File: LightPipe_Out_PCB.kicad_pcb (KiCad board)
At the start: 4 copper layers, 38.1 x 38.1 mm, 11 parts, among them J1 Conn_01x03, J2 Conn_01x02, J3 Conn_01x04, J4 Conn_01x04, J5 Conn_01x04, J6 Conn_01x01, J7 Conn_01x01, J8 Conn_01x02, J9 Conn_01x03, M1 MountingHole_3.2mm_M3, M2 MountingHole_3.2mm_M3

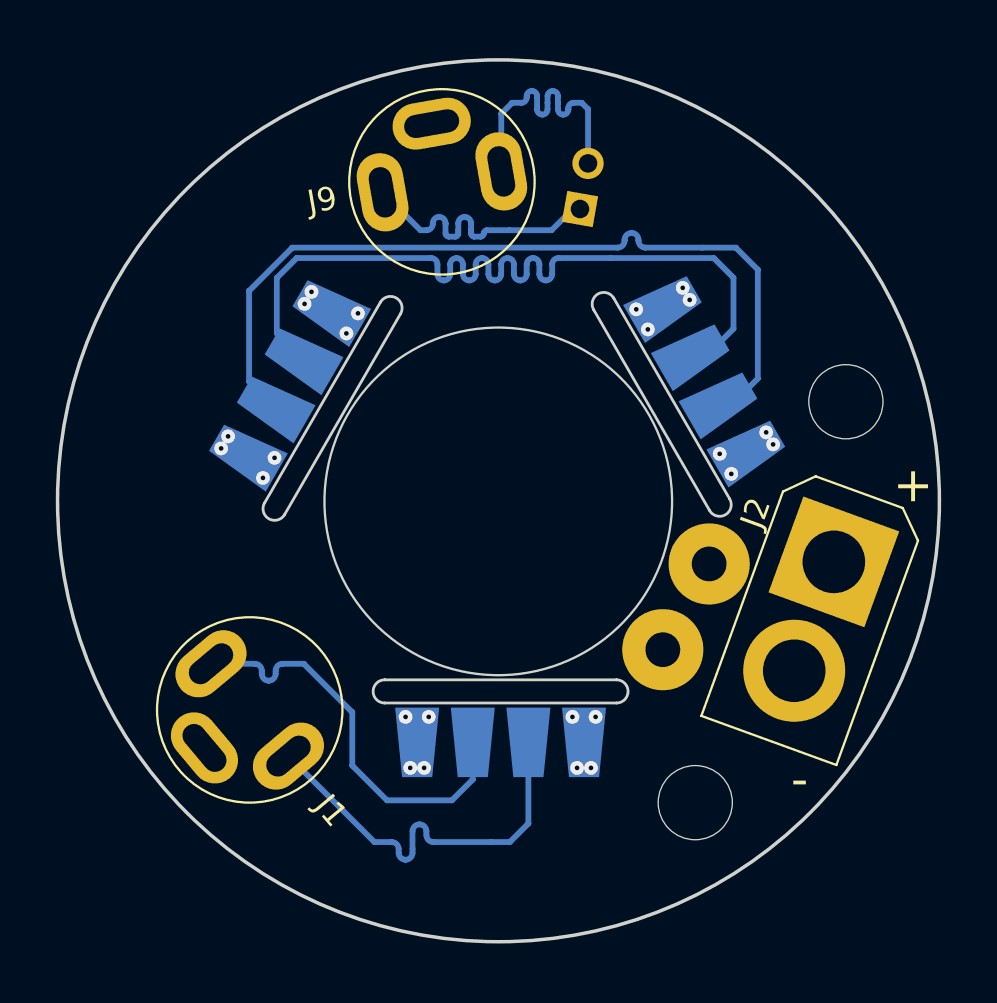
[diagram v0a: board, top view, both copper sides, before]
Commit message: [PCB] New Design features to use the PCB as In- and Out-PCB
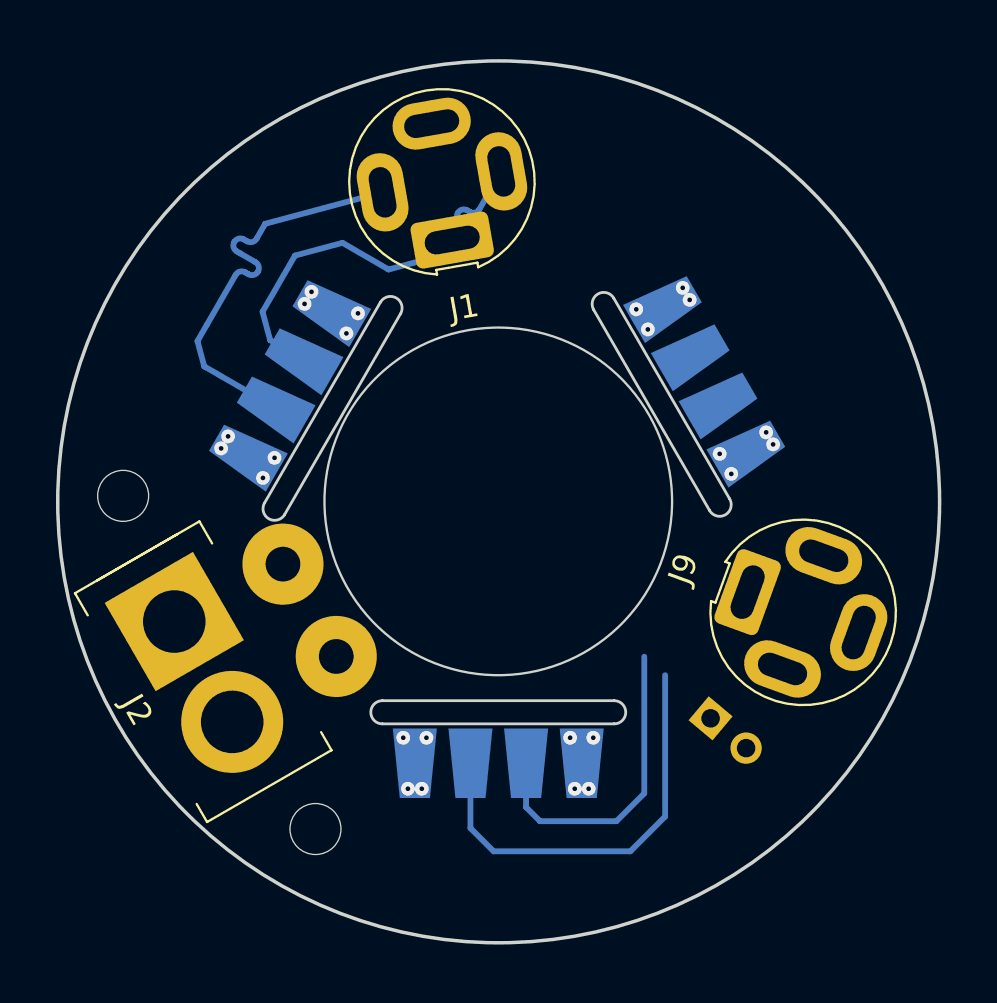
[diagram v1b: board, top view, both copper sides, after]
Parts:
- removed M2: MountingHole_3.2mm_M3, MountingHole:MountingHole_3.2mm_M3
- added REF**: MountingHole_2.2mm_M2, MountingHole:MountingHole_2.2mm_M2, F.Cu at (-16.2, -0.24)
- J1, J9: value Conn_01x03 -> Conn_01x04; footprint h8-Connectors:Lumberg-KLB-4-Klinkensteckverbinder-3_5 -> h8-Connectors:Lumberg-KLB-4-Klinkensteckverbinder-3_5-180deg-turnable
- M1: value MountingHole_3.2mm_M3 -> MountingHole_2.2mm_M2; footprint MountingHole:MountingHole_3.2mm_M3 -> MountingHole:MountingHole_2.2mm_M2
- moved M1 29.4 mm to (-7.89, 14.1), turned to -60 degrees
- moved J2 26.5 mm to (-12.7, 7.35), turned to -60 degrees
- moved J9 24.2 mm to (13.2, 4.79), turned to -110 degrees
- moved J1 24.2 mm to (-2.43, -13.8), turned to 10 degrees
- moved J8 22.7 mm to (9.16, 9.36), turned to -130 degrees
- moved J6 18.4 mm to (-9.29, 2.71), turned to -60 degrees
- moved J4 16.3 mm to (0.00, 9.80), turned to -90 degrees
- moved J3 15.4 mm to (7.66, -4.54), turned to 30 degrees
- moved J5 15.4 mm to (-7.76, -4.36), turned to 150 degrees
- moved J7 14.1 mm to (-6.99, 6.69), turned to -60 degrees
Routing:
- net /d1: track 38.0 -> 13.6 mm
- net /clk1: track 37.0 -> 18.3 mm
- net /clk3: track 12.0 -> 0.00 mm
- net /d3: track 11.9 -> 0.00 mm
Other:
- outline, holes or cut-outs redrawn
- board text removed: "+"
- board text removed: "-"

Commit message: Changed designators from J? to X? and LD? | Improved Footprints
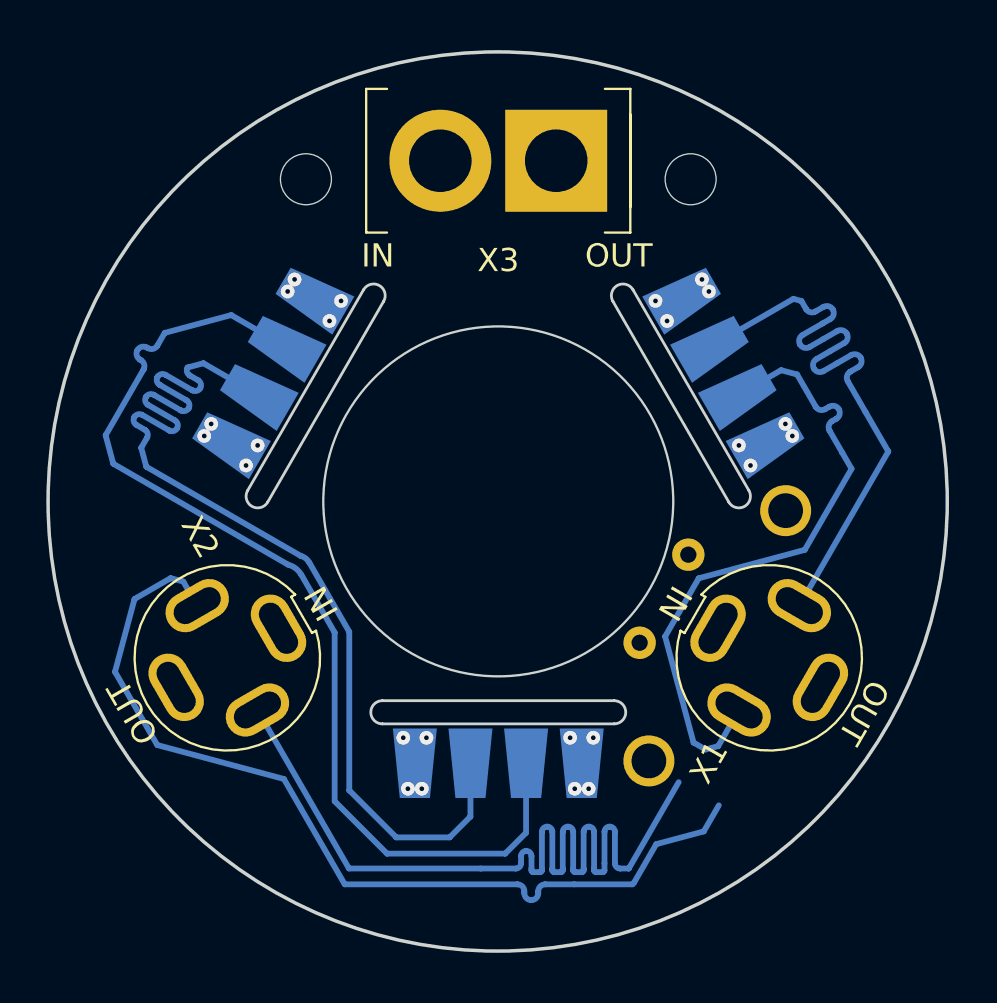
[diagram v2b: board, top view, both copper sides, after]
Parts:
- removed J8: Conn_01x02, Connector_PinHeader_2.00mm:PinHeader_1x02_P2.00mm_Vertical
- added X4.1: Conn_01x01, Connector_Wire:SolderWire-0.15sqmm_1x01_D0.5mm_OD1.5mm, B.Cu at (6.10, 6.10)
- added X4.2: Conn_01x01, Connector_Wire:SolderWire-0.15sqmm_1x01_D0.5mm_OD1.5mm, B.Cu at (8.20, 2.30)
- moved M1 28.0 mm to (-8.30, -13.9), turned to 180 degrees
- moved REF** 28.0 mm to (8.30, -13.9), turned to 180 degrees
- moved X3 25.5 mm to (0.00, -14.7), turned to 180 degrees
- moved X2 24.9 mm to (-11.7, 6.75), turned to 120 degrees
- moved X1 24.9 mm to (11.7, 6.75), turned to -120 degrees
- moved X5.1 20.4 mm to (12.4, 0.40), turned to 60 degrees
- moved X5.2 17.9 mm to (6.50, 11.2), turned to 60 degrees
- moved LD2 17.0 mm to (-8.49, -4.90), turned to 150 degrees
- moved LD3 16.3 mm to (0.00, 9.80), turned to -90 degrees
- moved LD1 16.3 mm to (8.49, -4.90), turned to 30 degrees
- renumbered J5 to LD1, J4 to LD2, J3 to LD3, J1 to X1, J9 to X2, J2 to X3, J7 to X5.1, J6 to X5.2
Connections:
- X3 pad 1: GND -> +5V
- X3 pad 2: +5V -> GND
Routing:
- net /d3: track 0.00 -> 40.0 mm
- net /clk3: track 0.00 -> 39.9 mm
- net /d1: track 13.6 -> 44.9 mm
- net /clk1: track 18.3 -> 44.9 mm
- net /d2: track 18.0 -> 28.0 mm
- net /clk2: track 17.9 -> 27.9 mm
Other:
- board size 38.1 x 38.1 mm -> 38.8 x 38.8 mm
- board text added: "IN"
- board text added: "OUT"

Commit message: [PCB] Improved footprints | optimized footprint locations | optimized wires
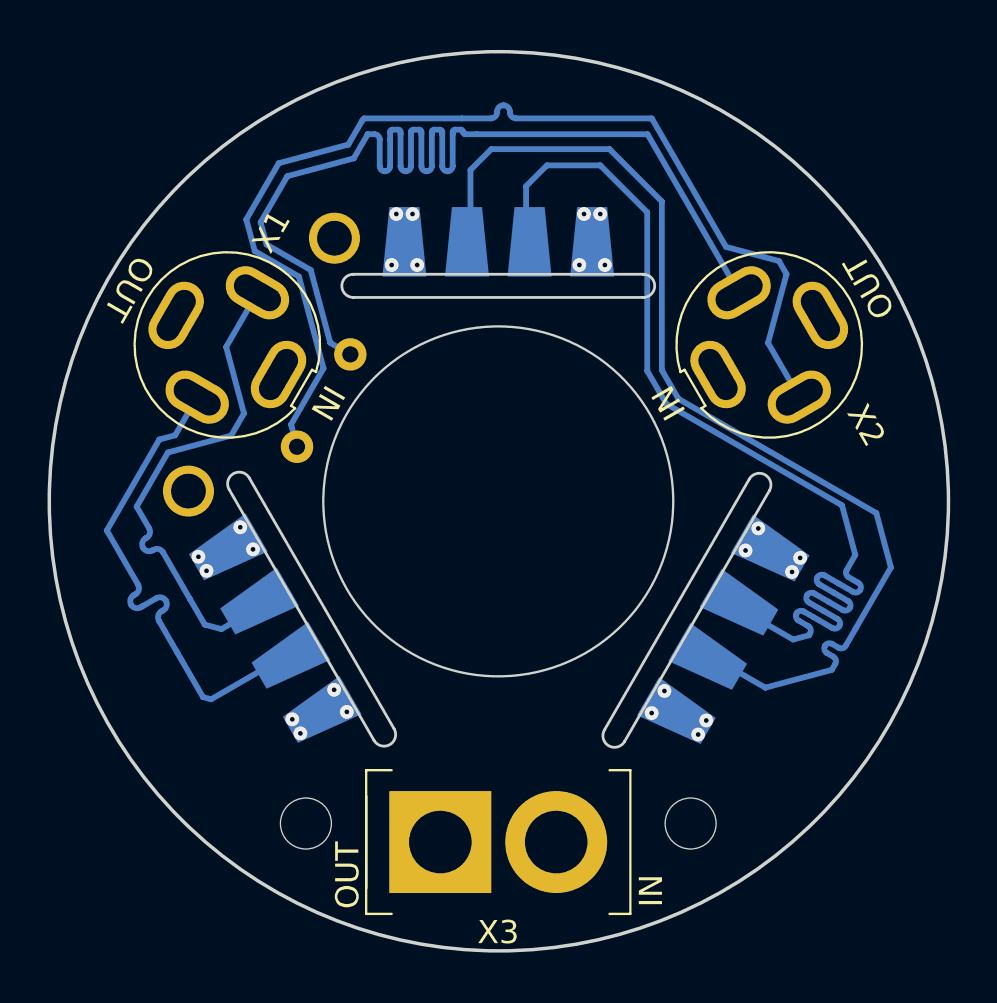
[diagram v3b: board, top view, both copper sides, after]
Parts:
- X4.1, X4.2: footprint Connector_Wire:SolderWire-0.15sqmm_1x01_D0.5mm_OD1.5mm -> h8-Connectors:Solder-Pad-THT-0.7mm
- X5.1, X5.2: footprint Connector_Wire:SolderWire-0.15sqmm_1x01_D0.5mm_OD1.5mm -> h8-Connectors:Solder-Pad-THT-1.5mm
- moved M1 32.4 mm to (8.30, 13.9), turned to 0 degrees
- moved REF** 32.4 mm to (-8.30, 13.9), turned to 0 degrees
- moved X3 29.4 mm to (0.00, 14.7), turned to 0 degrees
- moved X1 27.0 mm to (-11.7, -6.75), turned to 60 degrees
- moved X2 27.0 mm to (11.7, -6.75), turned to -60 degrees
- moved X5.2 26.3 mm to (-7.07, -11.4), turned to -120 degrees
- moved X5.1 25.8 mm to (-13.4, -0.44), turned to -120 degrees
- moved LD1 19.6 mm to (-8.49, 4.90), turned to -150 degrees
- moved LD2 19.6 mm to (8.49, 4.90), turned to -30 degrees
- moved LD3 19.6 mm to (0.00, -9.80), turned to 90 degrees
- moved X4.1 17.6 mm to (-6.38, -6.34), turned to -120 degrees
- moved X4.2 17.5 mm to (-8.68, -2.36), turned to -120 degrees
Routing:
- net /clk3: track 39.9 -> 46.9 mm
- net /d3: track 40.0 -> 47.0 mm
- net /d2: track 28.0 -> 21.5 mm
- net /clk2: track 27.9 -> 21.4 mm
- net /d1: track 44.9 -> 45.4 mm
- net /clk1: track 44.9 -> 45.5 mm
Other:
- outline, holes or cut-outs redrawn

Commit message: [doc] Create KiBot export and a basic documentation in README.md
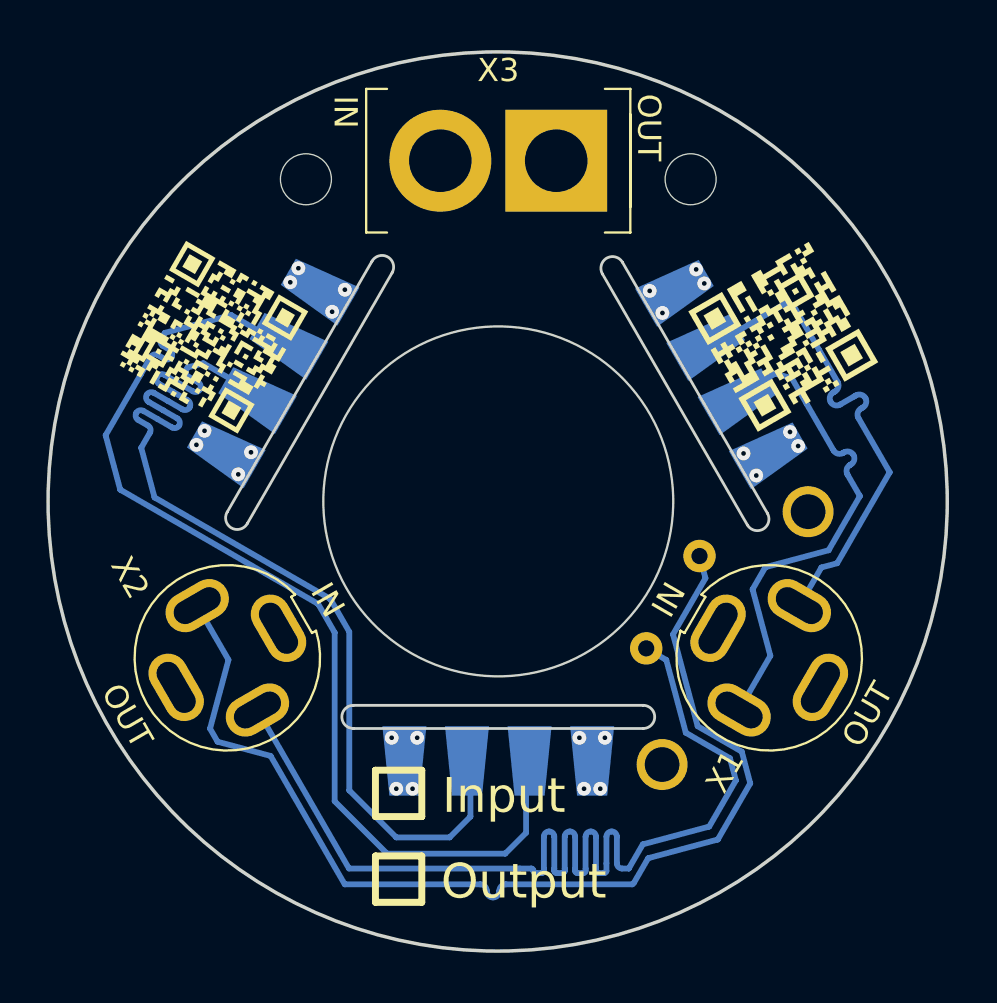
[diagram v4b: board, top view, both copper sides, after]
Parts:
- added QR***: QR_ProjecData, QR_Lib:QR_ProjecData, F.Cu at (12.3, -7.10)
- added QR***: QR_WebUrl, QR_Lib:QR_WebUrl, F.Cu at (-12.3, -7.10)
- moved M1 32.4 mm to (-8.30, -13.9), turned to 180 degrees
- moved REF** 32.4 mm to (8.30, -13.9), turned to 180 degrees
- moved X3 29.4 mm to (0.00, -14.7), turned to 180 degrees
- moved X1 27.0 mm to (11.7, 6.75), turned to -120 degrees
- moved X2 27.0 mm to (-11.7, 6.75), turned to 120 degrees
- moved X5.1 26.8 mm to (13.4, 0.44), turned to 60 degrees
- moved X5.2 26.8 mm to (7.07, 11.4), turned to 60 degrees
- moved LD1 19.6 mm to (8.49, -4.90), turned to 30 degrees
- moved LD2 19.6 mm to (-8.49, -4.90), turned to 150 degrees
- moved LD3 19.6 mm to (0.00, 9.80), turned to -90 degrees
- moved X4.2 18.0 mm to (8.68, 2.36), turned to 60 degrees
- moved X4.1 18.0 mm to (6.38, 6.34), turned to 60 degrees
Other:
- outline, holes or cut-outs redrawn
- board text added: "Input"
- board text added: "Output"

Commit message: [QR] Added QR-Code to schematic | defined QR-Code on Board to be not on schematic
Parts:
- renumbered QR*** to QR1, QR*** to QR2
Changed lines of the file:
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@@
   (footprint "QR_Lib:QR_ProjecData" (layer "F.Cu")
     (at 12.297561 -7.1 120)
-    (attr exclude_from_pos_files exclude_from_bom)
-    (fp_text reference "QR***" (at 0 4.25 120) (layer "F.SilkS") hide
+    (attr board_only exclude_from_pos_files exclude_from_bom)
+    (fp_text reference "QR1" (at 0 4.25 120) (layer "F.SilkS") hide
       (effects (font (size 1 1) (thickness 0.15)))
     )
@@
   (footprint "QR_Lib:QR_WebUrl" (layer "F.Cu")
     (at -12.297561 -7.1 -120)
-    (attr exclude_from_pos_files exclude_from_bom)
-    (fp_text reference "QR***" (at 0 4.25 60) (layer "F.SilkS") hide
+    (attr board_only exclude_from_pos_files exclude_from_bom)
+    (fp_text reference "QR2" (at 0 4.25 60) (layer "F.SilkS") hide
       (effects (font (size 1 1) (thickness 0.15)))
     )

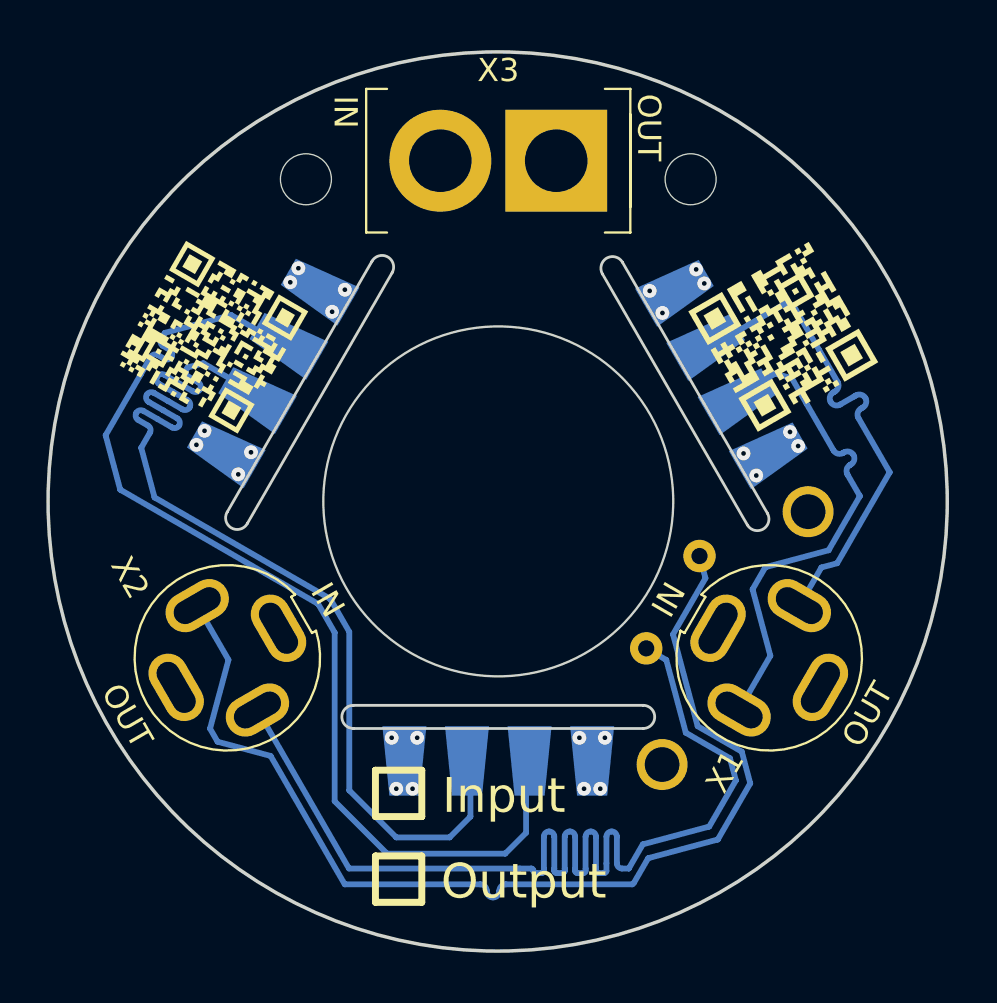
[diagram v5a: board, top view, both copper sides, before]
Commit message: [pcb] Optimized X1 and X2 positon
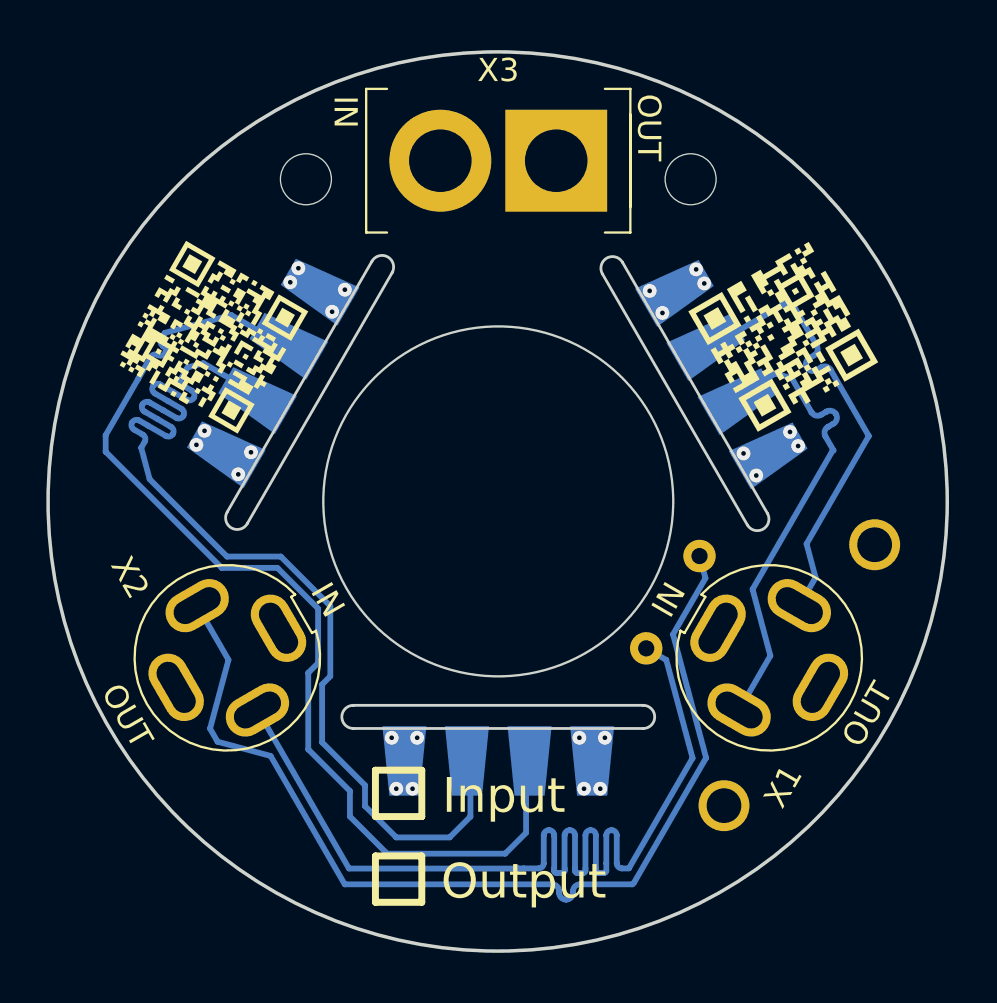
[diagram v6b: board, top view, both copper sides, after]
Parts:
- LD1, LD2, LD3: value Conn_01x04 -> APA102
- M1: renamed from REF**; value MountingHole_2.2mm_M2 -> 2.2mm_M2
- M2: renamed from M1; value MountingHole_2.2mm_M2 -> 2.2mm_M2
- X1, X2: value Conn_01x04 -> KLB-4
- X3: value Conn_01x02 -> XT30
- X4.1, X4.2: value Conn_01x01 -> Cable-0.7mm
- X5.1, X5.2: value Conn_01x01 -> Cable-1.5mm
- moved X5.1 3.21 mm to (16.2, 1.87)
- moved X5.2 3.21 mm to (9.74, 13.1)
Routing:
- net /d3: track 47.0 -> 44.0 mm
- net /clk3: track 46.9 -> 43.9 mm
- net /d2: track 21.5 -> 20.0 mm
- net /clk2: track 21.4 -> 20.0 mm
